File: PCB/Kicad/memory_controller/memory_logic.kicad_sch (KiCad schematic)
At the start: 4 parts, among them U21 4xAND__SN74HC08DR, U22 6xNOT__SN74HC14DR

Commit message: fix
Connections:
- net memory_logic_OUT: no longer names the net of U21.8 (3Y), U22.5 (3A)
- net muxnOE_n renamed ~{OE}_MUX_n
- net muxnOE_p renamed ~{OE}_MUX_p
- net nWE_mem renamed ~{WE}_mem
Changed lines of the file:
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@@
-	)
-	(junction
-		(at 120.65 60.96)
-		(diameter 0)
-		(color 0 0 0 0)
 	)
 	(junction
@@
 	(wire
 		(pts
-			(xy 120.65 60.96) (xy 123.19 60.96)
-		)
-		(stroke
-			(width 0)
-			(type default)
-		)
-	)
-	(wire
-		(pts
 			(xy 110.49 58.42) (xy 118.11 58.42)
 		)
@@
 		)
 	)
-	(hierarchical_label "muxnOE_n"
+	(hierarchical_label "~{OE}_MUX_n"
 		(shape output)
 		(at 121.92 111.76 0)
@@
 		)
 	)
-	(hierarchical_label "memory_logic_OUT"
-		(shape output)
-		(at 123.19 60.96 0)
-		(effects
-			(font
-				(size 1.27 1.27)
-			)
-			(justify left)
-		)
-	)
-	(hierarchical_label "muxnOE_p"
+	(hierarchical_label "~{OE}_MUX_p"
 		(shape input)
 		(at 62.23 111.76 180)
@@
 		)
 	)
-	(hierarchical_label "nWE_mem"
+	(hierarchical_label "~{WE}_mem"
 		(shape output)
 		(at 121.92 114.3 0)

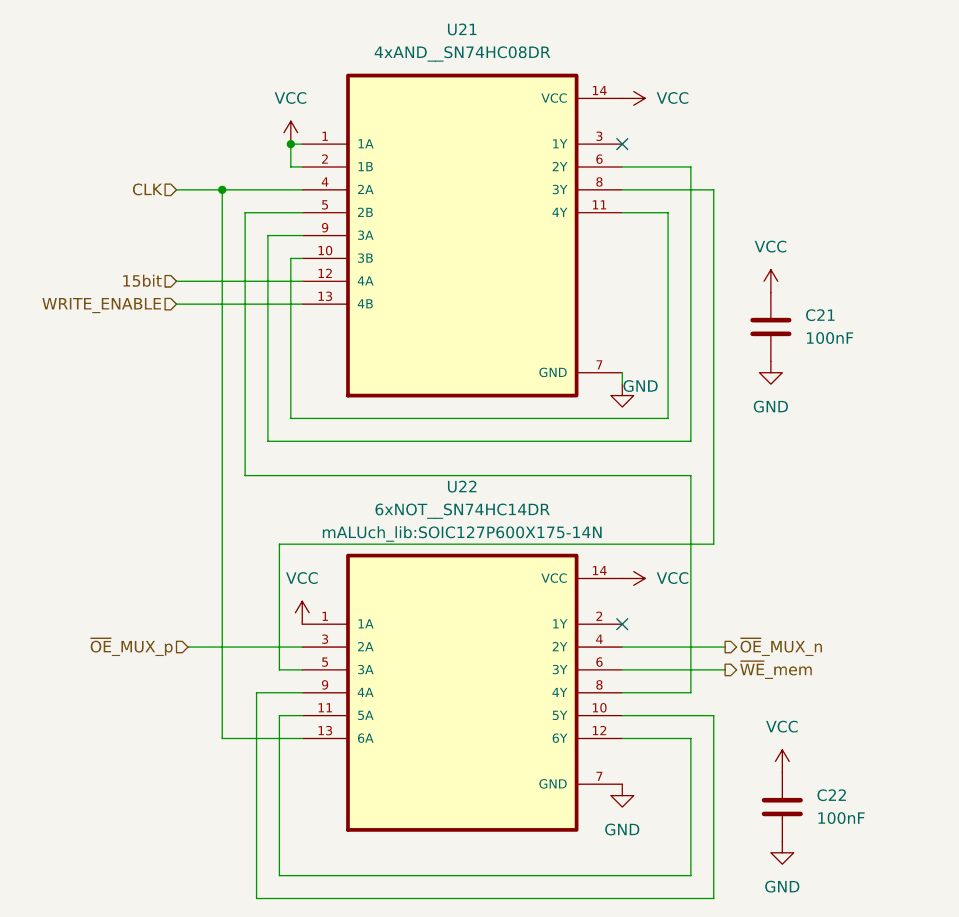
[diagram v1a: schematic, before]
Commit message: memory controler fix
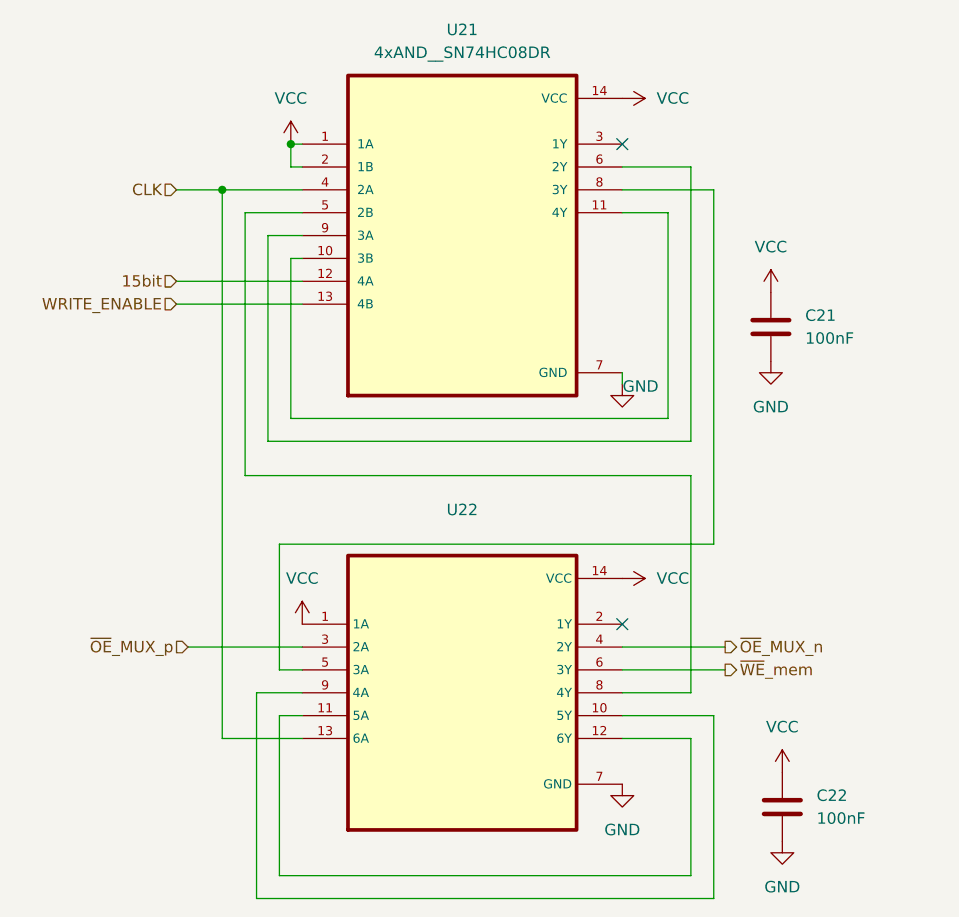
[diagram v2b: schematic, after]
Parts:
- removed U22: 6xNOT__SN74HC14DR, mALUch_lib:SOIC127P600X175-14N, symbol mALUch_lib:6xNOT__SN74HC14DR
- added U22: ~, mALUch_lib:SOIC127P600X175-14N, symbol mALUch_lib:6xNOT__SN74HC04DR
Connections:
- net CLK: now also U22.13 (6A)
- net GND: now also U22.7 (GND)
- net VCC: now also U22.1 (1A), U22.14 (VCC)
- net ~{OE}_MUX_n: now also U22.4 (2Y)
- net ~{OE}_MUX_p: now also U22.3 (2A)
- net ~{WE}_mem: now also U22.6 (3Y)
- net at U21.8 (3Y): now also U22.5 (3A)
- net at U21.5 (2B): now also U22.8 (4Y)
- new net: U22.10 (5Y), U22.9 (4A)
- new net: U22.11 (5A), U22.12 (6Y)

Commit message: kicad fix
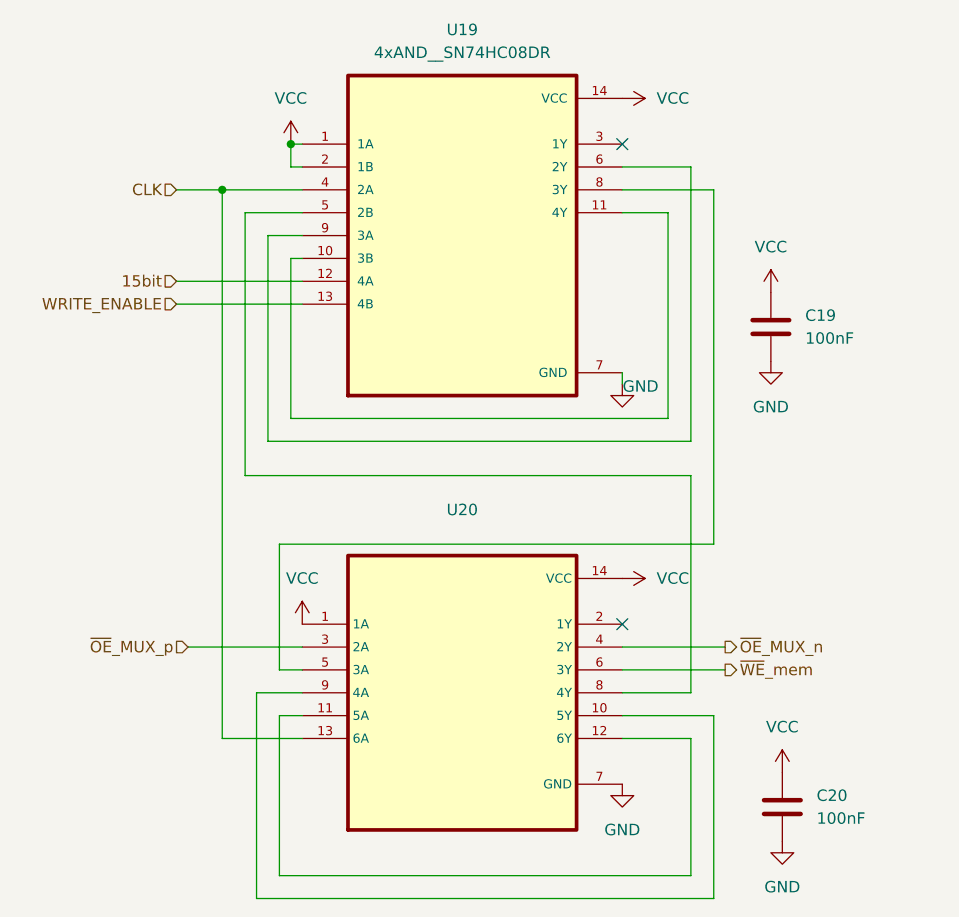
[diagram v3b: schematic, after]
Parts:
- renumbered C21 to C19, C22 to C20, U21 to U19, U22 to U20
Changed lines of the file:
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@@
 		(dnp no)
 		(fields_autoplaced yes)
-		(property "Reference" "C21"
+		(property "Reference" "C19"
 			(at 130.81 74.9299 0)
 			(effects
@@
 			(project "memory_controller"
 				(path "/dccec861-b967-466c-843e-d6d1ad6064ce/be370388-1dae-49ce-b017-0586b8e562a1"
-					(reference "C21")
+					(reference "C19")
 					(unit 1)
 				)
@@
 		(dnp no)
 		(fields_autoplaced yes)
-		(property "Reference" "#PWR0105"
+		(property "Reference" "#PWR095"
 			(at 73.66 59.69 0)
 			(effects
@@
 			(project "memory_controller"
 				(path "/dccec861-b967-466c-843e-d6d1ad6064ce/be370388-1dae-49ce-b017-0586b8e562a1"
-					(reference "#PWR0105")
+					(reference "#PWR095")
 					(unit 1)
 				)
@@
 		(dnp no)
 		(fields_autoplaced yes)
-		(property "Reference" "C22"
+		(property "Reference" "C20"
 			(at 132.08 128.2699 0)
 			(effects
@@
 			(project "memory_controller"
 				(path "/dccec861-b967-466c-843e-d6d1ad6064ce/be370388-1dae-49ce-b017-0586b8e562a1"
-					(reference "C22")
+					(reference "C20")
 					(unit 1)
 				)
@@
 		(dnp no)
 		(fields_autoplaced yes)
-		(property "Reference" "#PWR0114"
+		(property "Reference" "#PWR0104"
 			(at 128.27 139.7 0)
 			(effects
@@
 			(project "memory_controller"
 				(path "/dccec861-b967-466c-843e-d6d1ad6064ce/be370388-1dae-49ce-b017-0586b8e562a1"
-					(reference "#PWR0114")
+					(reference "#PWR0104")
 					(unit 1)
 				)
@@
 		(dnp no)
 		(fields_autoplaced yes)
-		(property "Reference" "#PWR0107"
+		(property "Reference" "#PWR097"
 			(at 106.68 50.8 0)
 			(effects
@@
 			(project "memory_controller"
 				(path "/dccec861-b967-466c-843e-d6d1ad6064ce/be370388-1dae-49ce-b017-0586b8e562a1"
-					(reference "#PWR0107")
+					(reference "#PWR097")
 					(unit 1)
 				)
@@
 		(dnp no)
 		(fields_autoplaced yes)
-		(property "Reference" "#PWR0113"
+		(property "Reference" "#PWR0103"
 			(at 128.27 129.54 0)
 			(effects
@@
 			(project "memory_controller"
 				(path "/dccec861-b967-466c-843e-d6d1ad6064ce/be370388-1dae-49ce-b017-0586b8e562a1"
-					(reference "#PWR0113")
+					(reference "#PWR0103")
 					(unit 1)
 				)
@@
 		(dnp no)
 		(fields_autoplaced yes)
-		(property "Reference" "U21"
+		(property "Reference" "U19"
 			(at 92.71 43.18 0)
 			(effects
@@
 			(project ""
 				(path "/dccec861-b967-466c-843e-d6d1ad6064ce/be370388-1dae-49ce-b017-0586b8e562a1"
-					(reference "U21")
+					(reference "U19")
 					(unit 1)
 				)
@@
 		(dnp no)
 		(fields_autoplaced yes)
-		(property "Reference" "#PWR0112"
+		(property "Reference" "#PWR0102"
 			(at 127 86.36 0)
 			(effects
@@
 			(project "memory_controller"
 				(path "/dccec861-b967-466c-843e-d6d1ad6064ce/be370388-1dae-49ce-b017-0586b8e562a1"
-					(reference "#PWR0112")
+					(reference "#PWR0102")
 					(unit 1)
 				)
@@
 		(dnp no)
 		(fields_autoplaced yes)
-		(property "Reference" "#PWR0111"
+		(property "Reference" "#PWR0101"
 			(at 127 76.2 0)
 			(effects
@@
 			(project "memory_controller"
 				(path "/dccec861-b967-466c-843e-d6d1ad6064ce/be370388-1dae-49ce-b017-0586b8e562a1"
-					(reference "#PWR0111")
+					(reference "#PWR0101")
 					(unit 1)
 				)
@@
 		(dnp no)
 		(fields_autoplaced yes)
-		(property "Reference" "U22"
+		(property "Reference" "U20"
 			(at 92.71 96.52 0)
 			(effects
@@
 			(project ""
 				(path "/dccec861-b967-466c-843e-d6d1ad6064ce/be370388-1dae-49ce-b017-0586b8e562a1"
-					(reference "U22")
+					(reference "U20")
 					(unit 1)
 				)
@@
 		(dnp no)
 		(fields_autoplaced yes)
-		(property "Reference" "#PWR0106"
+		(property "Reference" "#PWR096"
 			(at 74.93 113.03 0)
 			(effects
@@
 			(project "memory_controller"
 				(path "/dccec861-b967-466c-843e-d6d1ad6064ce/be370388-1dae-49ce-b017-0586b8e562a1"
-					(reference "#PWR0106")
+					(reference "#PWR096")
 					(unit 1)
 				)
@@
 		(on_board yes)
 		(dnp no)
-		(property "Reference" "#PWR0108"
+		(property "Reference" "#PWR098"
 			(at 110.49 88.9 0)
 			(effects
@@
 			(project "memory_controller"
 				(path "/dccec861-b967-466c-843e-d6d1ad6064ce/be370388-1dae-49ce-b017-0586b8e562a1"
-					(reference "#PWR0108")
+					(reference "#PWR098")
 					(unit 1)
 				)
@@
 		(dnp no)
 		(fields_autoplaced yes)
-		(property "Reference" "#PWR0110"
+		(property "Reference" "#PWR0100"
 			(at 110.49 133.35 0)
 			(effects
@@
 			(project ""
 				(path "/dccec861-b967-466c-843e-d6d1ad6064ce/be370388-1dae-49ce-b017-0586b8e562a1"
-					(reference "#PWR0110")
+					(reference "#PWR0100")
 					(unit 1)
 				)
@@
 		(dnp no)
 		(fields_autoplaced yes)
-		(property "Reference" "#PWR0109"
+		(property "Reference" "#PWR099"
 			(at 106.68 104.14 0)
 			(effects
@@
 			(project ""
 				(path "/dccec861-b967-466c-843e-d6d1ad6064ce/be370388-1dae-49ce-b017-0586b8e562a1"
-					(reference "#PWR0109")
-					(unit 1)
-				)
+					(reference "#PWR099")
+					(unit 1)
+				)

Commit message: pcb init
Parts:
- C19, C20: footprint (none) -> Capacitor_SMD:C_0402_1005Metric
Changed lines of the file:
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@@
 			)
 		)
-		(property "Footprint" ""
+		(property "Footprint" "Capacitor_SMD:C_0402_1005Metric"
 			(at 126.0348 72.39 0)
 			(effects
@@
 			)
 		)
-		(property "Footprint" ""
+		(property "Footprint" "Capacitor_SMD:C_0402_1005Metric"
 			(at 127.3048 125.73 0)
 			(effects

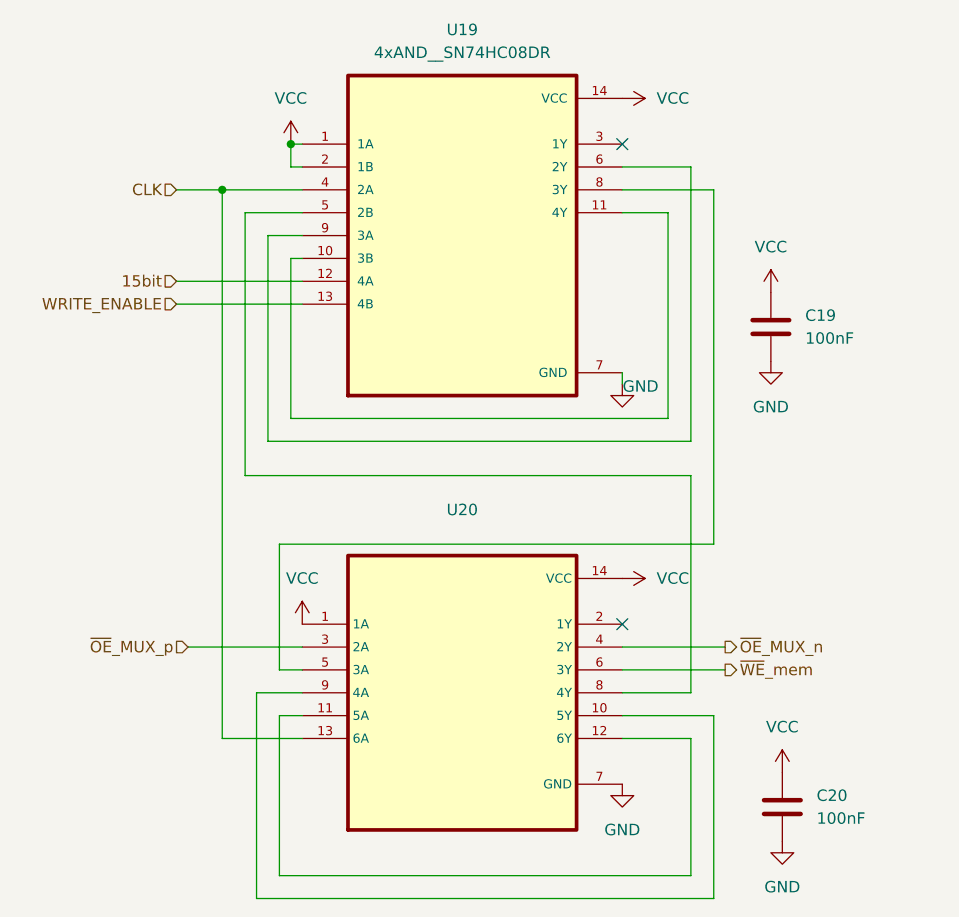
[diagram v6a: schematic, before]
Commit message: memory controller schematic update
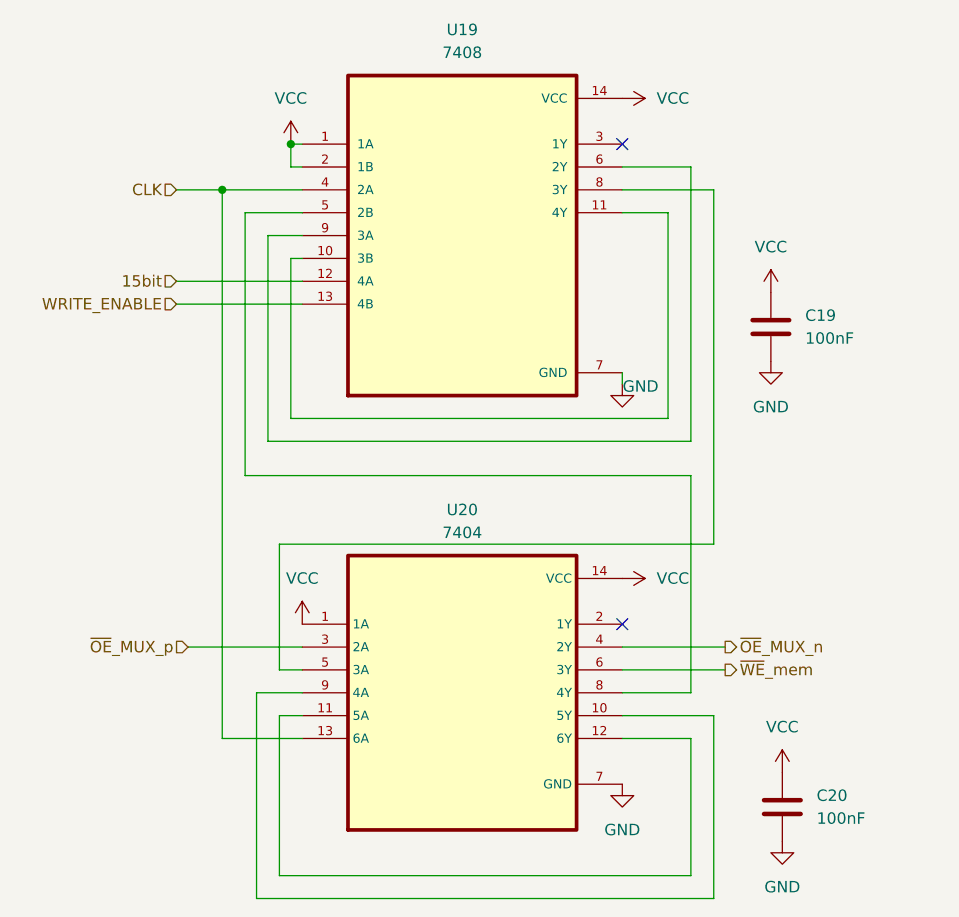
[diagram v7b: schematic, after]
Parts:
- U19: value 4xAND__SN74HC08DR -> 7408; footprint mALUch_lib:SOIC127P600X175-14N -> Package_SO:SO-14_3.9x8.65mm_P1.27mm
- U20: value ~ -> 7404; footprint mALUch_lib:SOIC127P600X175-14N -> Package_SO:SO-14_3.9x8.65mm_P1.27mm
